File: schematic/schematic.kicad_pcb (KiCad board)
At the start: 4 copper layers, 100 x 100 mm, 262 parts, among them J1 Conn_01x04, J10 Conn_01x03, J11 Conn_01x02, J12 Conn_01x02, J13 Conn_01x02, J14 Conn_01x02, J15 Conn_01x02, J16 Conn_01x02, J17 Conn_01x04, J18 Conn_02x13_Odd_Even, J19 Conn_02x05_Odd_Even, J2 Conn_01x04, J20 Conn_02x05_Odd_Even, J3 Conn_01x04, J4 Conn_01x04, J5 Conn_01x04, J6 Conn_01x06, J7 Conn_01x03, J8 Screw_Terminal_01x02, J9 Conn_01x03, Q1 PSMN1R7-30YL, Q2 PSMN1R7-30YL, Q3 NCV8402, Q4 NCV8402, SW1 SW_Push_Dual, SW2 SW_DIP_x03, U1 STM32F401VETx, U2 TMC2130, U3 TMC2130, U4 TMC2130, U5 TMC2130, U6 BD9E302EFJ, U7 BD9E302EFJ, U8 BD9E302EFJ, Y1 Crystal_GND24

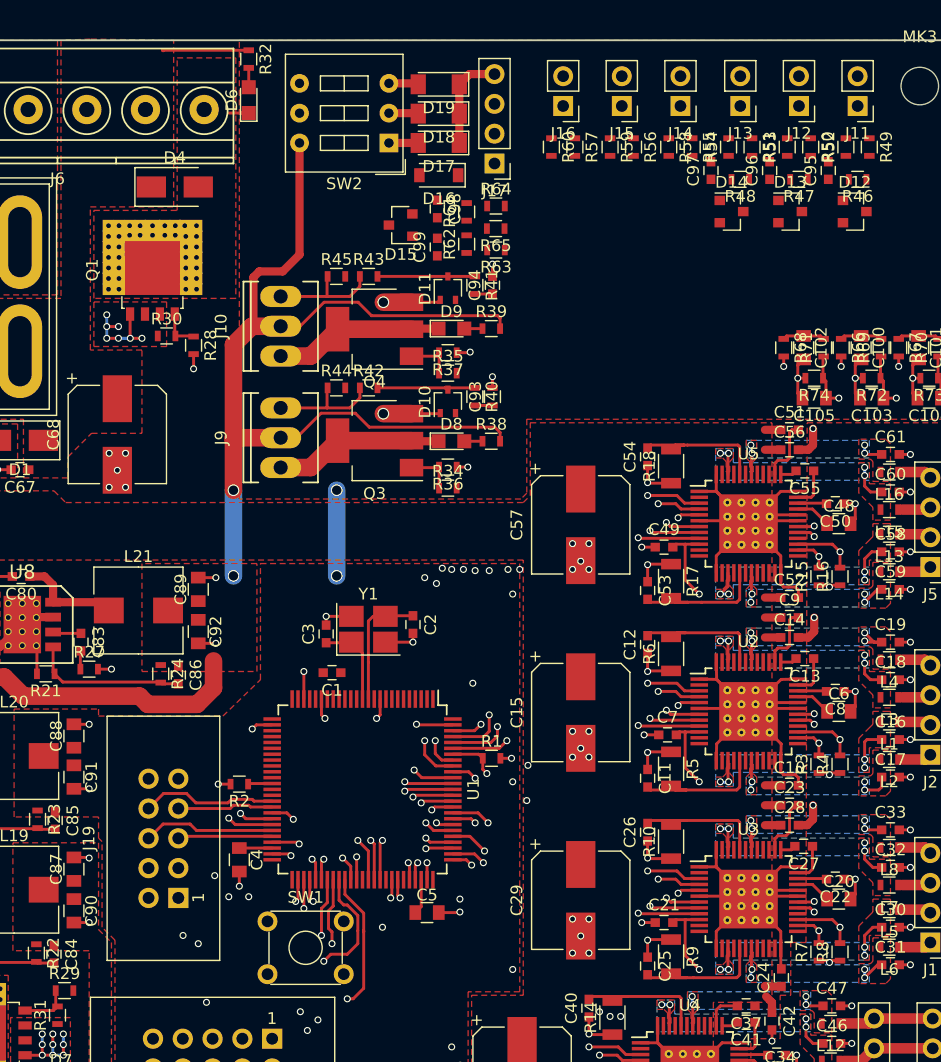
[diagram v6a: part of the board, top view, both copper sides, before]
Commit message: Routed signals to pi connector
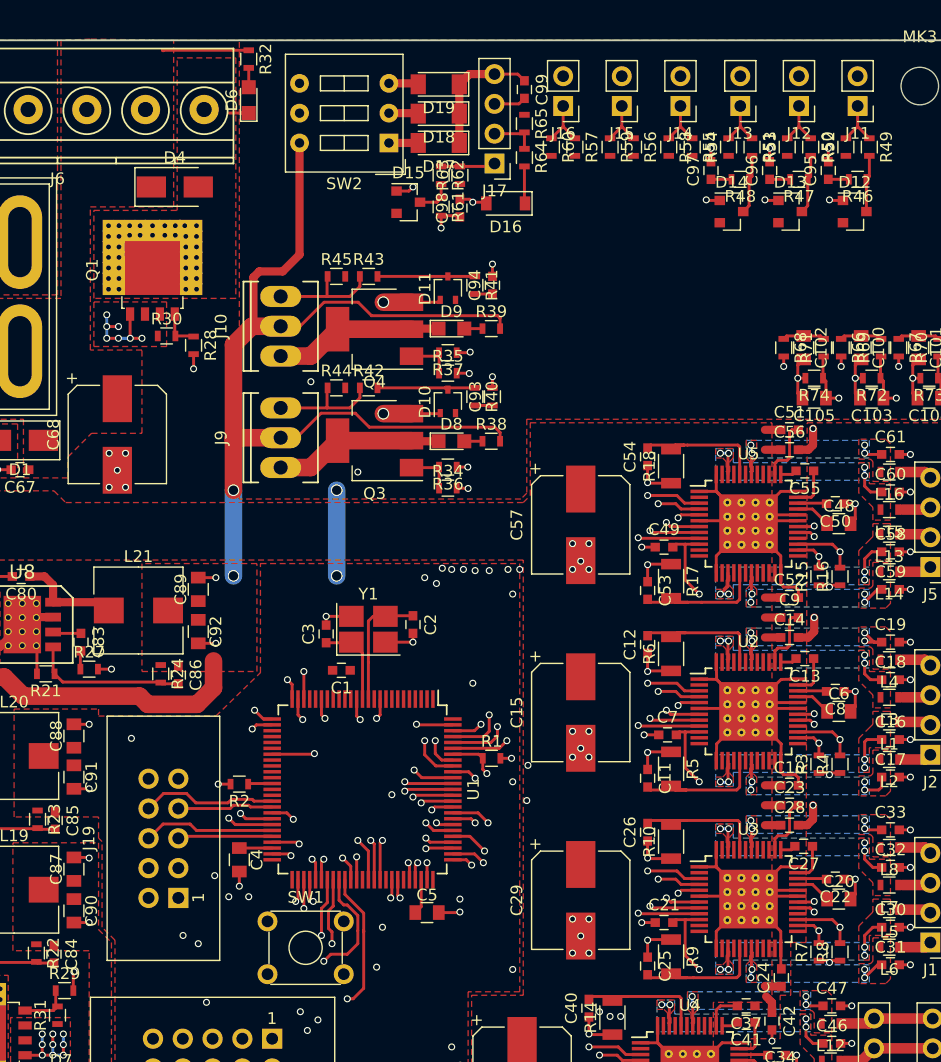
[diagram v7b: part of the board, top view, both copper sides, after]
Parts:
- moved C99 15.3 mm to (227.5, 54.2), turned to 270 degrees
- moved R65 9.28 mm to (227.5, 57.1), turned to 270 degrees
- moved R63 7.08 mm to (222.0, 61.5), turned to 90 degrees
- moved R62 6.26 mm to (220.4, 61.5), turned to 270 degrees
- moved D16 6.18 mm to (225.9, 63.9)
- moved R64 4.79 mm to (227.5, 60.0), turned to 270 degrees
- moved R61 2.22 mm to (220.4, 64.2), turned to 270 degrees
- moved D15 2.06 mm to (217.6, 63.8), turned to 0 degrees
- moved C98 1.93 mm to (222.0, 64.3), turned to 90 degrees
- moved C1 0.82 mm to (211.9, 103.7)
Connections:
- net Net-(U1-Pad4) renamed ZSTOP
- U1 pad 1: Net-(U1-Pad1) -> ZEND
- U1 pad 2: Net-(U1-Pad2) -> YEND
- U1 pad 23: BPWM -> F0PWM
- U1 pad 25: F0PWM -> F1PWM
- U1 pad 26: F1PWM -> BPWM
- U1 pad 3: Net-(U1-Pad3) -> XEND
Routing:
- net THERM3: track 0.00 -> 57.7 mm, vias 0 -> 2
- net RST: track 4.73 -> 53.4 mm, vias 0 -> 3
- net F1PWM: track 0.00 -> 42.9 mm, vias 0 -> 3
- net EPWM: track 0.00 -> 42.3 mm, vias 0 -> 3
- net F0PWM: track 0.00 -> 33.6 mm, vias 0 -> 3
- net GND: track 390.1 -> 403.8 mm, vias 123 -> 131
- net Net-(D14-Pad3): track 0.00 -> 5.06 mm
- net Net-(D13-Pad3): track 0.00 -> 5.06 mm
- net Net-(D12-Pad3): track 0.00 -> 4.85 mm
- net Net-(J17-Pad1): track 0.00 -> 4.65 mm
- net Net-(J16-Pad1): track 0.00 -> 4.58 mm
- net Net-(J15-Pad1): track 0.00 -> 4.58 mm
- net Net-(J14-Pad1): track 0.00 -> 4.58 mm
- net Net-(J13-Pad1): track 0.00 -> 4.58 mm
- net Net-(J12-Pad1): track 0.00 -> 4.58 mm
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
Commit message: Saved layout
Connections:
- J18 pad 13: BOOT1 -> Net-(J18-Pad13)
- R2 pad 1: BOOT1 -> Net-(R2-Pad1)
- U1 pad 37: BOOT1 -> Net-(R2-Pad1)
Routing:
- net RST: track 53.4 -> 57.9 mm
- net Net-(R2-Pad1): track 0.00 -> 2.07 mm
- net BOOT1: track 2.07 -> 0.00 mm
